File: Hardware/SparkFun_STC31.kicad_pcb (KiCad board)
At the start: 2 copper layers, 25.4 x 25.4 mm, 47 parts, among them J3 Qwiic_RA, J4 I2C, J5 Qwiic_RA, U1 STC31, U2 SHTC3

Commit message: Finishes routing the board, adds silk
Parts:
- removed the G*** at (162.0, 73.7) (x2)
- removed kibuzzard-680A784B: G***, kibuzzard-680A784B
- removed kibuzzard-680BA25F: G***, kibuzzard-680BA25F
- added G***: LOGO, SparkFun-Aesthetic:SparkFun_Logo_NoFlame_9mm, F.Cu at (136.0, 87.2)
- added G***: LOGO, SparkFun-Aesthetic:SparkFun_Logo_NoFlame_9mm, B.Cu at (136.0, 87.2)
- added kibuzzard-68139425: G***, kibuzzard-68139425, B.Cu at (143.9, 104.1)
- added kibuzzard-6813D00F: G***, kibuzzard-6813D00F, F.Cu at (143.6, 105.6)
- added kibuzzard-6813D00F: G***, kibuzzard-6813D00F, B.Cu at (144.4, 105.5)
- added kibuzzard-6813D10D: G***, kibuzzard-6813D10D, B.Cu at (132.9, 99.4)
- added kibuzzard-6813D116: G***, kibuzzard-6813D116, B.Cu at (133.0, 101.7)
- added kibuzzard-6813D11F: G***, kibuzzard-6813D11F, B.Cu at (133.0, 103.9)
- added kibuzzard-6813D1B2: G***, kibuzzard-6813D1B2, B.Cu at (136.0, 97.5)
- moved kibuzzard-68139425 33.8 mm to (144.1, 104.2)
- moved Ref** 17.4 mm to (129.4, 109.4)
- moved kibuzzard-67D9D97F 0.19 mm to (142.2, 92.7)
- turned C3 to 90 degrees
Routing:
- net ADDR: track 0.00 -> 16.4 mm, vias 0 -> 1
- net 3.3V: track 52.9 -> 61.8 mm, vias 2 -> 4
- net SDA: track 56.6 -> 57.9 mm
- net SCL: track 59.2 -> 60.1 mm
- net GND: track 3.42 -> 2.87 mm, vias 18 -> 22

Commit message: Moves things ever so slightly
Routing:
- net GND: vias 22 -> 23

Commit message: Fix silk
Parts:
- removed R7, R8: 4.7k, SparkFun-Resistor:R_0603_1608Metric
- removed kibuzzard-68139425 (x2): G***, kibuzzard-68139425
- added R2: 2.2k, SparkFun-Resistor:R_0603_1608Metric, F.Cu at (144.5, 92.9)
- added R3: 2.2k, SparkFun-Resistor:R_0603_1608Metric, F.Cu at (146.1, 92.9)
- added kibuzzard-682CCCFC: G***, kibuzzard-682CCCFC, F.Cu at (142.8, 104.6)
- added kibuzzard-682CCCFC: G***, kibuzzard-682CCCFC, B.Cu at (145.8, 104.6)
- added kibuzzard-682CCD34: G***, kibuzzard-682CCD34, F.Cu at (144.2, 104.2)
- added kibuzzard-682CCD34: G***, kibuzzard-682CCD34, B.Cu at (144.4, 104.3)

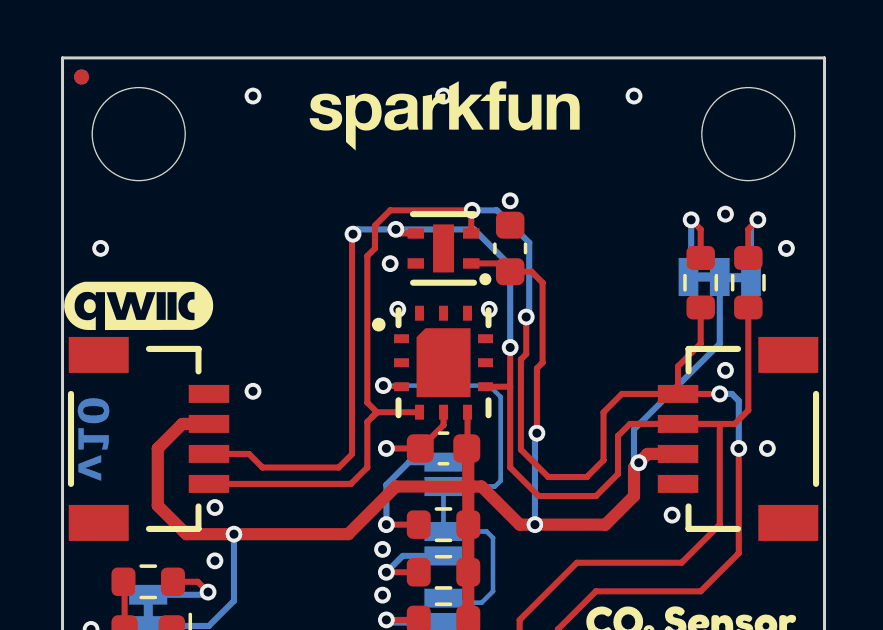
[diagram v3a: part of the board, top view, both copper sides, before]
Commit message: Replaces STC31 and SHTC3 with updated symbols/footprints
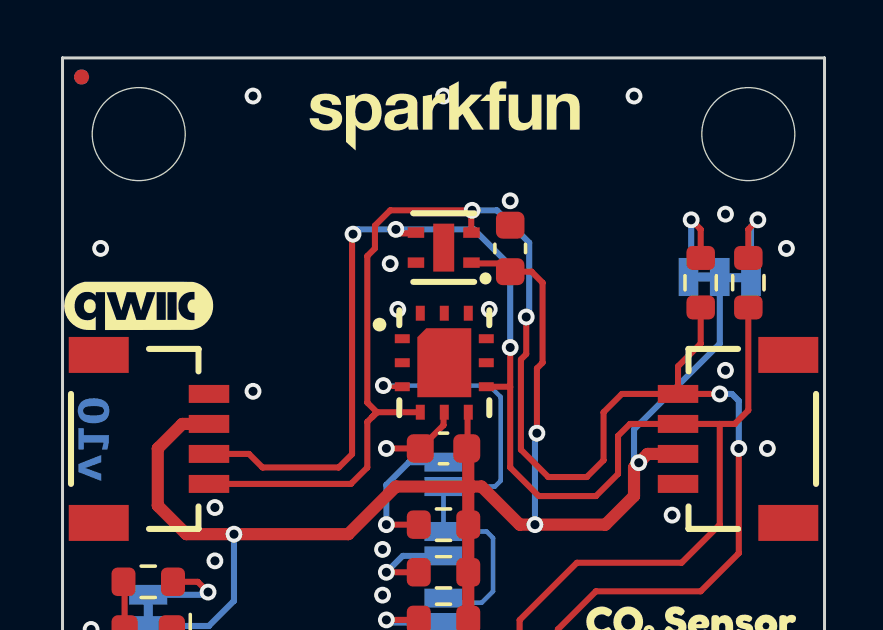
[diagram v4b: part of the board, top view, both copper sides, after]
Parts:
- removed U1: STC31, SparkFun-Sensor:STC31
- removed U2: SHTC3, SparkFun-Sensor:SHTC3
- added U3: STC31, SparkFun-Sensor:STC31, F.Cu at (136.1, 95.4)
- added U4: SHTC3, SparkFun-Sensor:SHTC3, F.Cu at (136.0, 91.8)
